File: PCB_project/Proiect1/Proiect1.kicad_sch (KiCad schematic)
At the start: 29 parts, among them J1 Conn_01x01_Pin, J2 Conn_01x01_Pin, J3 Conn_01x01_Pin, J4 Conn_01x01_Pin, Q1 BS170FTA, Q10 BS170FTA, Q11 BS250FTA, Q12 BS170FTA, Q13 BS170FTA, Q2 BS170FTA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

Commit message: Started new PCB
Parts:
- removed C2: 1n, Capacitor_SMD:C_0805_2012Metric, symbol Device:C
- removed Q1, Q10, Q12, Q13, Q2, Q4, Q6, Q7: BS170FTA, Package_TO_SOT_SMD:SOT-23, symbol Transistor_FET:BS170F
- removed Q11, Q3, Q5, Q8, Q9: BS250FTA, Package_TO_SOT_SMD:SOT-23, symbol Transistor_FET:BS250
- added D1, D2: 1N4148W, Diode_SMD:D_0805_2012Metric, symbol Diode:1N4148W
- added Q1, Q10, Q11, Q4, Q6, Q7, Q8, Q9: BC846, Package_TO_SOT_SMD:SOT-23, symbol Transistor_BJT:BC846
- added Q12, Q13, Q2, Q3, Q5: BC856, Package_TO_SOT_SMD:SOT-23, symbol Transistor_BJT:BC856
- added R10: 1k, Resistor_SMD:R_0805_2012Metric, symbol Device:R
- added R11, R12: 47k, Resistor_SMD:R_0805_2012Metric, symbol Device:R
- added R7, R8: 220k, Resistor_SMD:R_0805_2012Metric, symbol Device:R
- added R9: 4k7, Resistor_SMD:R_0805_2012Metric, symbol Device:R
- C1: value 1n -> 4n7; TME https://www.tme.eu/ro/en/details/grm2165c2a102ja01d/mlcc-sm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 -> (none)
- J1: value Conn_01x01_Pin -> Output; footprint Connector_PinHeader_2.54mm:PinHeader_1x01_P2.54mm_Vertical -> Connector_PinHeader_2.00mm:PinHeader_1x01_P2.00mm_Vertical
- J2, J4: value Conn_01x01_Pin -> GND; footprint Connector_PinHeader_2.54mm:PinHeader_1x01_P2.54mm_Vertical -> Connector_PinHeader_2.00mm:PinHeader_1x01_P2.00mm_Vertical
- J3: value Conn_01x01_Pin -> +25V; footprint Connector_PinHeader_2.54mm:PinHeader_1x01_P2.54mm_Vertical -> Connector_PinHeader_2.00mm:PinHeader_1x01_P2.00mm_Vertical
- R1: value 47k -> 2k; TME https://www.tme.eu/ro/en/details/erj6geyj473v/smd-resistors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 -> (none)
- R2: value 47k -> 220k; TME https://www.tme.eu/ro/en/details/erj6geyj473v/smd-resistors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 -> (none)
- R3: value 4k7 -> 2k; TME https://www.tme.eu/ro/en/details/erjp06j472v/smd-resistors/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 -> (none)
- R4: value 1k -> 220k; TME https://www.tme.eu/ro/en/details/rc0805fr-071k/smd-resistor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 -> (none)
- R5, R6: value 4k7 -> 47k; TME https://www.tme.eu/ro/en/details/erjp06j472v/smd-resistors/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 -> (none)
- RV1, RV2, RV3: footprint zCustom_Footprints:3361P_1 -> Potentiometer_SMD:Potentiometer_Vishay_TS53YL_Vertical; TME https://www.tme.eu/ro/en/details/3361p-1-104glf/single-turn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 -> (none)
- Rload1: TME https://www.tme.eu/ro/en/details/erj6geyj223v/smd-resistors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 -> (none)
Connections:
- net +25V: now also J3.1 (Pin_1), D2.2 (A), Q1.3 (C), Q12.2 (E), Q13.2 (E), Q2.2 (E), Q3.2 (E), R11.2, R9.2; no longer J1.1 (Pin_1), R1.1, R3.1
- net GND: now also D1.1 (K), Q10.2 (E), Q11.2 (E), Q6.2 (E), Q7.2 (E), R12.1; no longer R2.2
- net at C1.1: now also Q1.1 (B), Q3.3 (C), Q6.3 (C), R7.2
- net at R4.2: now also R3.2, RV3.2, RV3.3
- net at RV2.1: now also R2.1, Q2.1 (B), Q2.3 (C), Q3.1 (B)
- net at RV2.2, RV2.3: now also R1.1, R2.2; no longer R6.1
- net at RV1.1: now also Q1.2 (E)
- net at RV1.2, RV1.3: now also J1.1 (Pin_1), Rload1.1; no longer R5.1
- net at R5.2: now also Q4.1 (B)
- net at RV3.1: now also R4.1, Q6.1 (B), Q7.1 (B), Q7.3 (C)
- net at R6.2: now also Q5.1 (B)
- new net: Q12.3 (C), Q8.3 (C), R10.2, R5.1, R6.1
- new net: Q8.1 (B), R7.1
- new net: Q10.3 (C), Q8.2 (E), Q9.2 (E)
- new net: D2.1 (K), Q5.2 (E)
- new net: Q5.3 (C), R3.1
- new net: Q10.1 (B), Q11.1 (B), Q11.3 (C), R9.1
- new net: R10.1, R11.1, R12.2, R8.1
- new net: Q4.3 (C), R1.2
- new net: Q12.1 (B), Q13.1 (B), Q13.3 (C), Q9.3 (C)
- new net: D1.2 (A), Q4.2 (E)
- new net: Q9.1 (B), R8.2
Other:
- note added: "Power Supply (25V single)"
- note added: "Proiect CEF 2 Generator reglabil de semnal triunghiular"
- company: (none) -> Fratu-Halunga Theodor (434C)
- title: (none) -> Proiect CEF 2 - Generator reglabil de semnal triunghiular

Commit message: Updated PCB to conform with Manufacturing Requirements
Changed trace widths form 20 mils to 16 mils. Changed via sizes from 0.5mm/1mm to 0.4mm/1mm. Changed edge clearance from 0.5mm to 1mm. Changed trace clearance from 5? mils to 14 mils. Added 3 fiducials of size 1mm/2mm.

Still need to see what is up with that MECHANIC layer. Need to generate a mechanical drawing for the board edge, a drill drawing, a drill table and a drill legend as well as a layer stackup (technically KiCad already did this for me automatically but I don't know if this needs to be included in this MECHANIC layer or not)
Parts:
- added FID1, FID2, FID3: Fiducial, Fiducial:Fiducial_1mm_Mask2mm, symbol Mechanical:Fiducial
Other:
- note added: "Fiducials & Mounting Holes"
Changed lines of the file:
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@@
 		)
 	)
+	(polyline
+		(pts
+			(xy 165.1 165.1) (xy 165.1 196.85)
+		)
+		(stroke
+			(width 0)
+			(type default)
+		)
+	)
 	(wire
 		(pts
@@
 		)
 	)
+	(polyline
+		(pts
+			(xy 101.6 165.1) (xy 101.6 196.85)
+		)
+		(stroke
+			(width 0)
+			(type default)
+		)
+	)
 	(wire
 		(pts
@@
 		)
 	)
+	(polyline
+		(pts
+			(xy 101.6 165.1) (xy 165.1 165.1)
+		)
+		(stroke
+			(width 0)
+			(type default)
+		)
+	)
 	(wire
 		(pts
@@
 		)
 	)
+	(text "Fiducials & Mounting Holes"
+		(exclude_from_sim no)
+		(at 133.35 168.91 0)
+		(effects
+			(font
+				(size 3 3)
+				(thickness 0.6)
+				(bold yes)
+			)
+		)
+	)
 	(symbol
 		(lib_id "Transistor_BJT:BC846")
@@
 	)
 	(symbol
+		(lib_id "Mechanical:Fiducial")
+		(at 109.22 181.61 0)
+		(unit 1)
+		(exclude_from_sim no)
+		(in_bom yes)
+		(on_board yes)
+		(dnp no)
+		(fields_autoplaced yes)
+		(property "Reference" "FID1"
+			(at 111.76 180.3399 0)
+			(effects
+				(font
+					(size 1.27 1.27)
+				)
+				(justify left)
+			)
+		)
+		(property "Value" "Fiducial"
+			(at 111.76 182.8799 0)
+			(effects
+				(font
+					(size 1.27 1.27)
+				)
+				(justify left)
+			)
+		)
+		(property "Footprint" "Fiducial:Fiducial_1mm_Mask2mm"
+			(at 109.22 181.61 0)
+			(effects
+				(font
+					(size 1.27 1.27)
+				)
+				(hide yes)
+			)
+		)
+		(property "Datasheet" "~"
+			(at 109.22 181.61 0)
+			(effects
+				(font
+					(size 1.27 1.27)
+				)
+				(hide yes)
+			)
+		)
+		(property "Description" "Fiducial Marker"
+			(at 109.22 181.61 0)
+			(effects
+				(font
+					(size 1.27 1.27)
+				)
+				(hide yes)
+			)
+		)
+		(instances
+			(project "Proiect1"
+				(path "/c68b5534-5b2d-4c05-9c42-f54d4d765f6e"
+					(reference "FID1")
+					(unit 1)
+				)
+			)
+		)
+	)
+	(symbol
 		(lib_id "power:+24V")
 		(at 46.99 162.56 0)
@@
 	)
 	(symbol
+		(lib_id "Mechanical:Fiducial")
+		(at 152.4 181.61 0)
+		(unit 1)
+		(exclude_from_sim no)
+		(in_bom yes)
+		(on_board yes)
+		(dnp no)
+		(fields_autoplaced yes)
+		(property "Reference" "FID3"
+			(at 154.94 180.3399 0)
+			(effects
+				(font
+					(size 1.27 1.27)
+				)
+				(justify left)
+			)
+		)
+		(property "Value" "Fiducial"
+			(at 154.94 182.8799 0)
+			(effects
+				(font
+					(size 1.27 1.27)
+				)
+				(justify left)
+			)
+		)
+		(property "Footprint" "Fiducial:Fiducial_1mm_Mask2mm"
+			(at 152.4 181.61 0)
+			(effects
+				(font
+					(size 1.27 1.27)
+				)
+				(hide yes)
+			)
+		)
+		(property "Datasheet" "~"
+			(at 152.4 181.61 0)
+			(effects
+				(font
+					(size 1.27 1.27)
+				)
+				(hide yes)
+			)
+		)
+		(property "Description" "Fiducial Marker"
+			(at 152.4 181.61 0)
+			(effects
+				(font
+					(size 1.27 1.27)
+				)
+				(hide yes)
+			)
+		)
+		(instances
+			(project "Proiect1"
+				(path "/c68b5534-5b2d-4c05-9c42-f54d4d765f6e"
+					(reference "FID3")
+					(unit 1)
+				)
+			)
+		)
+	)
+	(symbol
 		(lib_id "Diode:1N4148W")
 		(at 180.34 105.41 90)
@@
 					(unit 1)
 				)
+			)
+		)
+	)
+	(symbol
+		(lib_id "Mechanical:Fiducial")
+		(at 130.81 181.61 0)
+		(unit 1)
+		(exclude_from_sim no)
+		(in_bom yes)
+		(on_board yes)
+		(dnp no)
+		(fields_autoplaced yes)
+		(property "Reference" "FID2"
+			(at 133.35 180.3399 0)
+			(effects
+				(font
+					(size 1.27 1.27)
+				)
+				(justify left)
+			)
+		)
+		(property "Value" "Fiducial"
+			(at 133.35 182.8799 0)
+			(effects
+				(font
+					(size 1.27 1.27)
+				)
+				(justify left)
+			)
+		)
+		(property "Footprint" "Fiducial:Fiducial_1mm_Mask2mm"
+			(at 130.81 181.61 0)
+			(effects
+				(font
+					(size 1.27 1.27)
+				)
+				(hide yes)
+			)
+		)
+		(property "Datasheet" "~"
+			(at 130.81 181.61 0)
+			(effects
+				(font
+					(size 1.27 1.27)
+				)
+				(hide yes)
+			)
+		)
+		(property "Description" "Fiducial Marker"
+			(at 130.81 181.61 0)
+			(effects
+				(font
+					(size 1.27 1.27)
+				)
+				(hide yes)
+			)
+		)
+		(instances
+			(project "Proiect1"
+				(path "/c68b5534-5b2d-4c05-9c42-f54d4d765f6e"
+					(reference "FID2")
+					(unit 1)
+				)

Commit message: Changed jumpers from THT to SMD
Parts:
- removed J1: Output, Connector_PinHeader_2.00mm:PinHeader_1x01_P2.00mm_Vertical, symbol Connector:Conn_01x01_Pin
- removed J2: GND, Connector_PinHeader_2.00mm:PinHeader_1x01_P2.00mm_Vertical, symbol Connector:Conn_01x01_Pin
- added J1: OUT, Connector_PinHeader_2.00mm:PinHeader_1x02_P2.00mm_Vertical_SMD_Pin1Left, symbol Connector:Conn_01x02_Pin
- J3, J4: footprint Connector_PinHeader_2.00mm:PinHeader_1x01_P2.00mm_Vertical -> Connector_PinHeader_2.00mm:PinHeader_1x02_P2.00mm_Vertical_SMD_Pin1Left; symbol Connector:Conn_01x01_Pin -> Connector:Conn_01x02_Pin
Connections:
- net +25V: now also J3.2 (Pin_2)
- net GND: now also J4.2 (Pin_2), J1.2 (Pin_2)
- net at RV1.2, RV1.3, Rload1.1: now also J1.1 (Pin_1)
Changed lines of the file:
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@@
 	)
 	(junction
+		(at 43.18 165.1)
+		(diameter 0)
+		(color 0 0 0 0)
+	)
+	(junction
 		(at 101.6 63.5)
 		(diameter 0)
 		(color 0 0 0 0)
 	)
+	(junction
+		(at 43.18 168.91)
+		(diameter 0)
+		(color 0 0 0 0)
+	)
 	(wire
 		(pts
@@
 	(wire
 		(pts
+			(xy 247.65 110.49) (xy 243.84 110.49)
+		)
+		(stroke
+			(width 0)
+			(type default)
+		)
+	)
+	(wire
+		(pts
+			(xy 43.18 168.91) (xy 43.18 171.45)
+		)
+		(stroke
+			(width 0)
+			(type default)
+		)
+	)
+	(wire
+		(pts
 			(xy 88.9 66.04) (xy 88.9 63.5)
 		)
@@
 	(wire
 		(pts
+			(xy 243.84 105.41) (xy 243.84 107.95)
+		)
+		(stroke
+			(width 0)
+			(type default)
+		)
+	)
+	(wire
+		(pts
 			(xy 180.34 26.67) (xy 180.34 25.4)
 		)
@@
 	(wire
 		(pts
+			(xy 43.18 162.56) (xy 43.18 165.1)
+		)
+		(stroke
+			(width 0)
+			(type default)
+		)
+	)
+	(wire
+		(pts
 			(xy 165.1 114.3) (xy 148.59 114.3)
 		)
@@
 	(wire
 		(pts
+			(xy 243.84 110.49) (xy 243.84 114.3)
+		)
+		(stroke
+			(width 0)
+			(type default)
+		)
+	)
+	(wire
+		(pts
 			(xy 171.45 46.99) (xy 171.45 48.26)
 		)
@@
 	(wire
 		(pts
+			(xy 247.65 107.95) (xy 243.84 107.95)
+		)
+		(stroke
+			(width 0)
+			(type default)
+		)
+	)
+	(wire
+		(pts
 			(xy 68.58 91.44) (xy 57.15 91.44)
 		)
@@
 	)
 	(symbol
+		(lib_id "Connector:Conn_01x02_Pin")
+		(at 252.73 107.95 0)
+		(mirror y)
+		(unit 1)
+		(exclude_from_sim no)
+		(in_bom yes)
+		(on_board yes)
+		(dnp no)
+		(property "Reference" "J1"
+			(at 256.032 107.95 0)
+			(effects
+				(font
+					(size 1.27 1.27)
+				)
+			)
+		)
+		(property "Value" "OUT"
+			(at 257.556 110.49 0)
+			(effects
+				(font
+					(size 1.27 1.27)
+				)
+			)
+		)
+		(property "Footprint" "Connector_PinHeader_2.00mm:PinHeader_1x02_P2.00mm_Vertical_SMD_Pin1Left"
+			(at 252.73 107.95 0)
+			(effects
+				(font
+					(size 1.27 1.27)
+				)
+				(hide yes)
+			)
+		)
+		(property "Datasheet" "~"
+			(at 252.73 107.95 0)
+			(effects
+				(font
+					(size 1.27 1.27)
+				)
+				(hide yes)
+			)
+		)
+		(property "Description" "Generic connector, single row, 01x02, script generated"
+			(at 252.73 107.95 0)
+			(effects
+				(font
+					(size 1.27 1.27)
+				)
+				(hide yes)
+			)
+		)
+		(pin "1"
+		)
+		(pin "2"
+		)
+		(instances
+			(project "Proiect1"
+				(path "/c68b5534-5b2d-4c05-9c42-f54d4d765f6e"
+					(reference "J1")
+					(unit 1)
+				)
+			)
+		)
+	)
+	(symbol
 		(lib_id "Device:R")
 		(at 168.91 114.3 90)
@@
 	)
 	(symbol
-		(lib_id "Connector:Conn_01x01_Pin")
-		(at 248.92 114.3 180)
-		(unit 1)
-		(exclude_from_sim no)
-		(in_bom yes)
-		(on_board yes)
-		(dnp no)
-		(property "Reference" "J2"
-			(at 248.285 119.38 0)
-			(effects
-				(font
-					(size 1.27 1.27)
-				)
-			)
-		)
-		(property "Value" "GND"
-			(at 248.285 116.84 0)
-			(effects
-				(font
-					(size 1.27 1.27)
-				)
-			)
-		)
-		(property "Footprint" "Connector_PinHeader_2.00mm:PinHeader_1x01_P2.00mm_Vertical"
-			(at 248.92 114.3 0)
-			(effects
-				(font
-					(size 1.27 1.27)
-				)
-				(hide yes)
-			)
-		)
-		(property "Datasheet" "~"
-			(at 248.92 114.3 0)
-			(effects
-				(font
-					(size 1.27 1.27)
-				)
-				(hide yes)
-			)
-		)
-		(property "Description" "Generic connector, single row, 01x01, script generated"
-			(at 248.92 114.3 0)
-			(effects
-				(font
-					(size 1.27 1.27)
-				)
-				(hide yes)
-			)
-		)
-		(pin "1"
-		)
-		(instances
-			(project "Proiect1"
-				(path "/c68b5534-5b2d-4c05-9c42-f54d4d765f6e"
-					(reference "J2")
-					(unit 1)
-				)
-			)
-		)
-	)
-	(symbol
 		(lib_id "Transistor_BJT:BC846")
 		(at 116.84 91.44 0)
@@
 	)
 	(symbol
-		(lib_id "Connector:Conn_01x01_Pin")
-		(at 248.92 105.41 0)
-		(mirror y)
-		(unit 1)
-		(exclude_from_sim no)
-		(in_bom yes)
-		(on_board yes)
-		(dnp no)
-		(property "Reference" "J1"
-			(at 248.285 100.33 0)
-			(effects
-				(font
-					(size 1.27 1.27)
-				)
-			)
-		)
-		(property "Value" "Output"
-			(at 248.285 102.87 0)
-			(effects
-				(font
-					(size 1.27 1.27)
-				)
-			)
-		)
-		(property "Footprint" "Connector_PinHeader_2.00mm:PinHeader_1x01_P2.00mm_Vertical"
-			(at 248.92 105.41 0)
-			(effects
-				(font
-					(size 1.27 1.27)
-				)
-				(hide yes)
-			)
-		)
-		(property "Datasheet" "~"
-			(at 248.92 105.41 0)
-			(effects
-				(font
-					(size 1.27 1.27)
-				)
-				(hide yes)
-			)
-		)
-		(property "Description" "Generic connector, single row, 01x01, script generated"
-			(at 248.92 105.41 0)
-			(effects
-				(font
-					(size 1.27 1.27)
-				)
-				(hide yes)
-			)
-		)
-		(pin "1"
-		)
-		(instances
-			(project "Proiect1"
-				(path "/c68b5534-5b2d-4c05-9c42-f54d4d765f6e"
-					(reference "J1")
-					(unit 1)
-				)
-			)
-		)
-	)
-	(symbol
 		(lib_id "Device:C")
 		(at 209.55 95.25 0)
@@
 	)
 	(symbol
-		(lib_id "Connector:Conn_01x01_Pin")
+		(lib_id "Connector:Conn_01x02_Pin")
 		(at 38.1 165.1 0)
+		(mirror x)
 		(unit 1)
 		(exclude_from_sim no)
@@
 		(dnp no)
 		(property "Reference" "J3"
-			(at 38.735 160.02 0)
+			(at 35.56 162.052 0)
 			(effects
 				(font
@@
 		)
 		(property "Value" "+25V"
-			(at 38.735 162.56 0)
+			(at 34.798 164.846 0)
 			(effects
 				(font
@@
 			)
 		)
-		(property "Footprint" "Connector_PinHeader_2.00mm:PinHeader_1x01_P2.00mm_Vertical"
+		(property "Footprint" "Connector_PinHeader_2.00mm:PinHeader_1x02_P2.00mm_Vertical_SMD_Pin1Left"
 			(at 38.1 165.1 0)
 			(effects
@@
 			)
 		)
-		(property "Description" "Generic connector, single row, 01x01, script generated"
+		(property "Description" "Generic connector, single row, 01x02, script generated"
 			(at 38.1 165.1 0)
 			(effects
@@
 		(pin "1"
 		)
+		(pin "2"
+		)
 		(instances
 			(project "Proiect1"
@@
 	)
 	(symbol
-		(lib_id "Connector:Conn_01x01_Pin")
+		(lib_id "Connector:Conn_01x02_Pin")
 		(at 38.1 168.91 0)
-		(mirror x)
 		(unit 1)
 		(exclude_from_sim no)
@@
 		(dnp no)
 		(property "Reference" "J4"
-			(at 38.735 173.99 0)
+			(at 35.306 168.91 0)
 			(effects
 				(font
@@
 		)
 		(property "Value" "GND"
-			(at 38.735 171.45 0)
+			(at 35.306 171.45 0)
 			(effects
 				(font
@@
 			)
 		)
-		(property "Footprint" "Connector_PinHeader_2.00mm:PinHeader_1x01_P2.00mm_Vertical"
+		(property "Footprint" "Connector_PinHeader_2.00mm:PinHeader_1x02_P2.00mm_Vertical_SMD_Pin1Left"
 			(at 38.1 168.91 0)
 			(effects
@@
 			)
 		)
-		(property "Description" "Generic connector, single row, 01x01, script generated"
+		(property "Description" "Generic connector, single row, 01x02, script generated"
 			(at 38.1 168.91 0)
 			(effects
@@
 		(pin "1"
 		)
+		(pin "2"
+		)
 		(instances

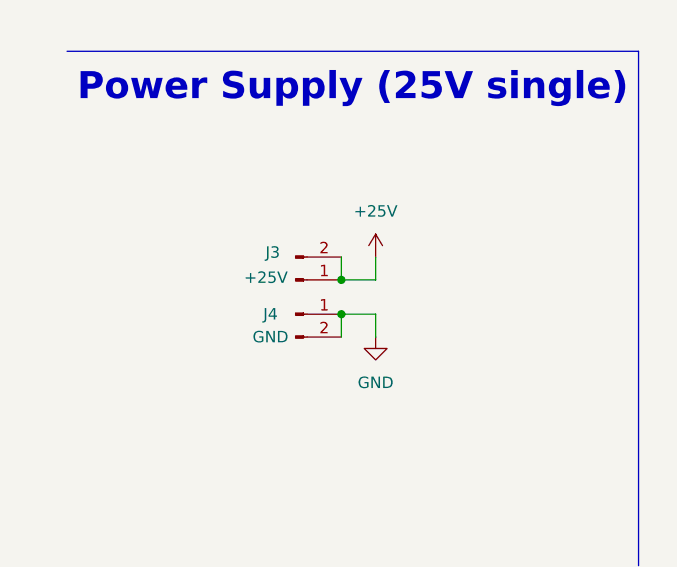
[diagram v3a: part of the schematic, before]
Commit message: Changed reference designators J3, J4 to J2, J3
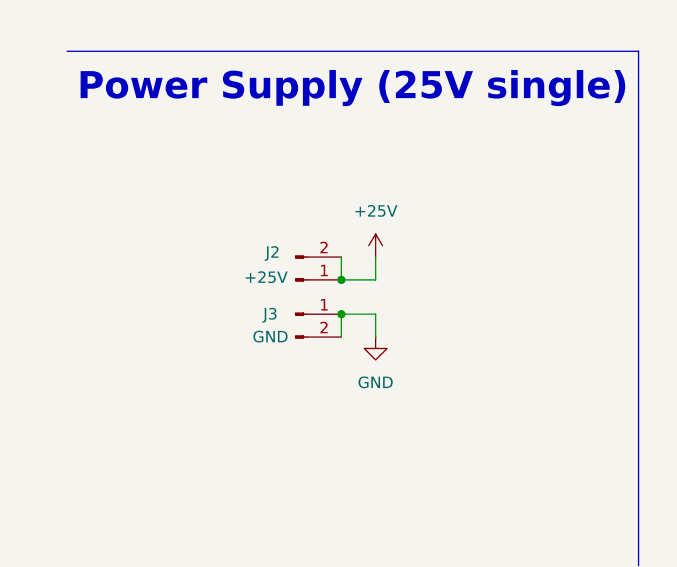
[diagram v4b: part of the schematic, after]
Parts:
- renumbered J3 to J2, J4 to J3
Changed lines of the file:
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@@
 		(on_board yes)
 		(dnp no)
-		(property "Reference" "J3"
+		(property "Reference" "J2"
 			(at 35.56 162.052 0)
 			(effects
@@
 			(project "Proiect1"
 				(path "/c68b5534-5b2d-4c05-9c42-f54d4d765f6e"
-					(reference "J3")
+					(reference "J2")
 					(unit 1)
 				)
@@
 		(on_board yes)
 		(dnp no)
-		(property "Reference" "J4"
+		(property "Reference" "J3"
 			(at 35.306 168.91 0)
 			(effects
@@
 			(project "Proiect1"
 				(path "/c68b5534-5b2d-4c05-9c42-f54d4d765f6e"
-					(reference "J4")
-					(unit 1)
-				)
+					(reference "J3")
+					(unit 1)
+				)

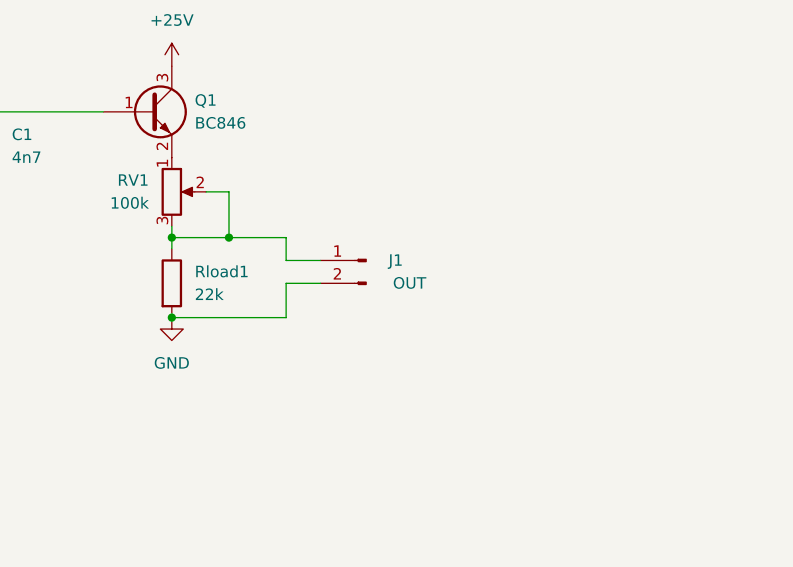
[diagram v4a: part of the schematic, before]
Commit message: Added Drill Table and simple stackup table
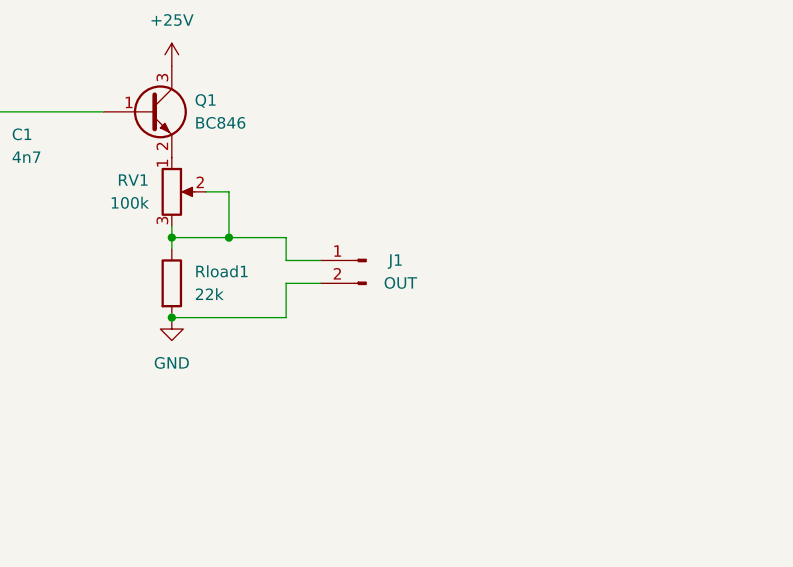
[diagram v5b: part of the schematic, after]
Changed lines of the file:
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@@
 		)
 		(property "Value" "OUT"
-			(at 257.556 110.49 0)
+			(at 256.54 110.49 0)
 			(effects
 				(font
